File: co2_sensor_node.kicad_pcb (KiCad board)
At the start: 4 copper layers, 100 x 100 mm, 122 parts, among them J1 Conn_01x03, J10 Conn_01x04, J11 Conn_01x06_Male, J12 Conn_01x02, J13 TF-15x15, J2 Conn_01x03, J3 Conn_01x02, J4 Conn_01x02, J5 Conn_01x03, J6 Conn_01x03, J7 Conn_01x02, J8 Conn_01x03, J9 Conn_01x04, Q1 AO3400A, Q2 AO3401A, Q3 AO3401A, Q4 AO3400A, SW1 K2-1102SP-C4SC-04, U1 TPS62130, U2 ESP32-WROOM-32D, U3 TC1508S

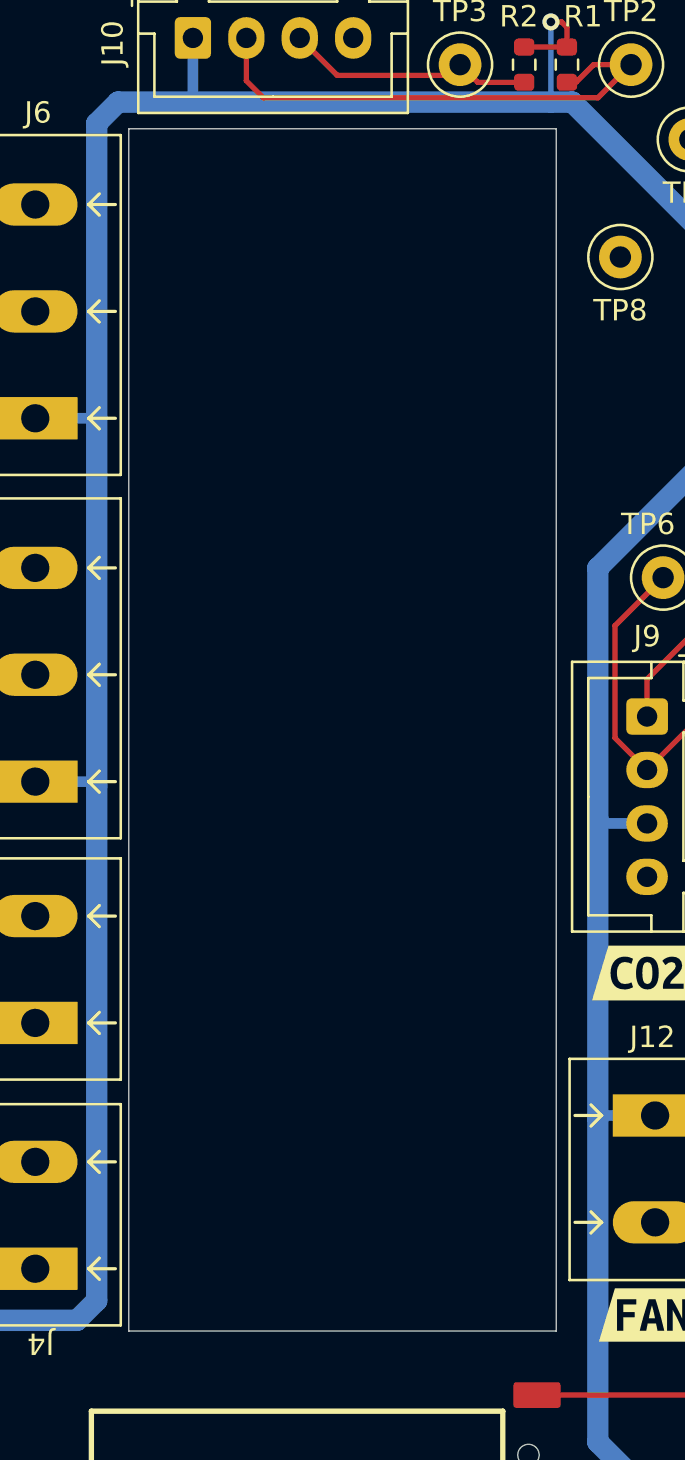
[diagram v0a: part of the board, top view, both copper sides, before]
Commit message: fixed the HOLE by adding rounded corners
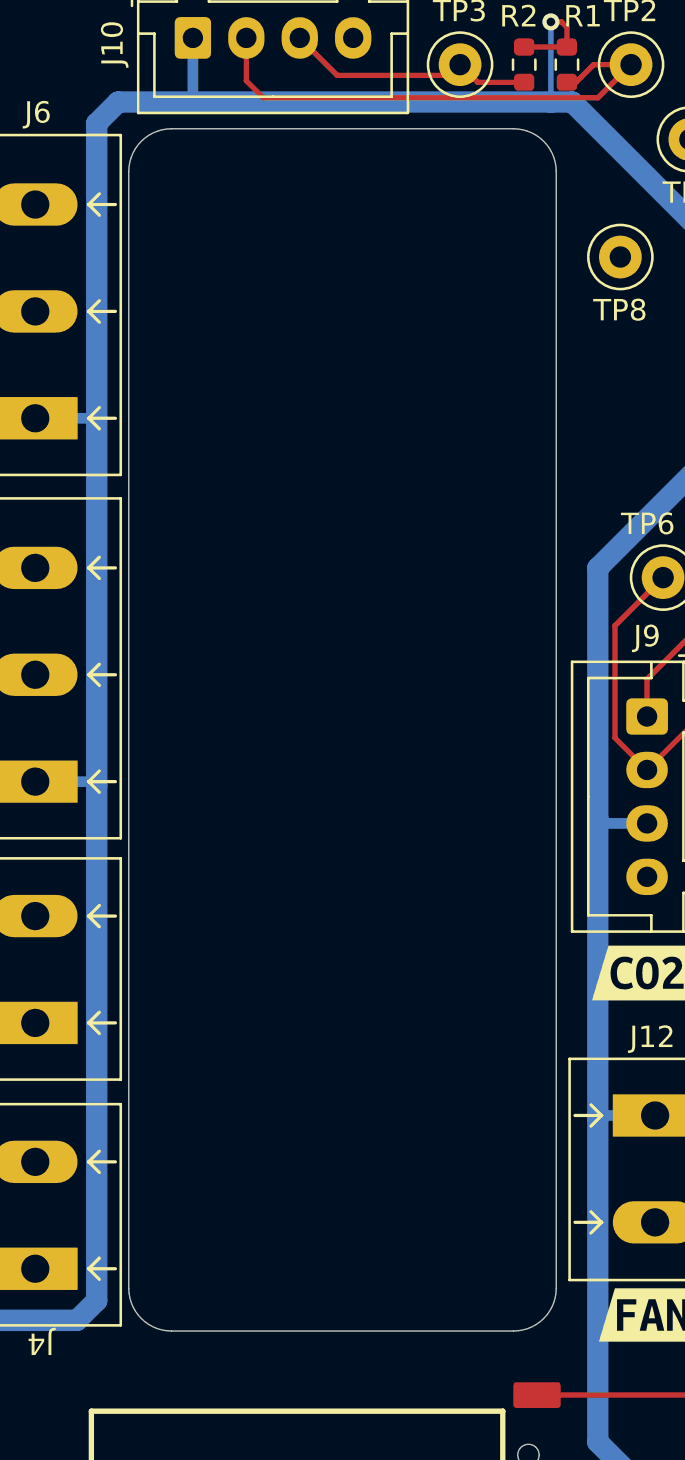
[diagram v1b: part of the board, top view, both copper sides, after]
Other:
- outline, holes or cut-outs redrawn
- board text added: "HOLE"
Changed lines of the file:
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@@
   )
   (gr_rect locked (start 148.5 135.5) (end 129.25 149.5) (layer "F.SilkS") (width 0.25) (fill none))
+  (gr_line (start 131 129.75) (end 131 77.5) (layer "Edge.Cuts") (width 0.05))
+  (gr_line (start 151 77.5) (end 151 129.75) (layer "Edge.Cuts") (width 0.05))
+  (gr_arc (start 133 131.75) (mid 131.585786 131.164214) (end 131 129.75) (layer "Edge.Cuts") (width 0.05))
   (gr_circle (center 150.5 105) (end 150.5 155) (layer "Edge.Cuts") (width 0.05) (fill none))
-  (gr_rect (start 131 75.5) (end 151 131.75) (layer "Edge.Cuts") (width 0.05) (fill none))
+  (gr_line (start 133 75.5) (end 149 75.5) (layer "Edge.Cuts") (width 0.05))
+  (gr_arc (start 149 75.5) (mid 150.414214 76.085786) (end 151 77.5) (layer "Edge.Cuts") (width 0.05))
+  (gr_arc (start 151 129.75) (mid 150.414214 131.164214) (end 149 131.75) (layer "Edge.Cuts") (width 0.05))
+  (gr_arc (start 131 77.5) (mid 131.585786 76.085786) (end 133 75.5) (layer "Edge.Cuts") (width 0.05))
+  (gr_line (start 149 131.75) (end 133 131.75) (layer "Edge.Cuts") (width 0.05))
+  (gr_text "HOLE" (at 140.9 104.2 90) (layer "Edge.Cuts")
+    (effects (font (size 5 5) (thickness 0.8)))
+  )
   (segment (start 115.75 121) (end 114.525 121) (width 0.25) (layer "F.Cu") (net 1))
   (segment (start 158.25 64.425) (end 158.25 63.25) (width 0.25) (layer "F.Cu") (net 1))
